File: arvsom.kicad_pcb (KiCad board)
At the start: 12 copper layers, 55 x 40 mm, 451 parts, among them J1 TAG-10PIN, J3 DF40C-100DP-0.4V(51), J4 DF40C-100DP-0.4V(51), Q1 DMG1013UWQ-7, Q5 DMG1012UW, U1 MT53D1024M32D4DT-053, U10 TDA19988BHN_C1,557, U11 KSZ9031RNXCA, U13 VIC7100, U2 GD25LQ256DWIGR, U3 MT53D1024M32D4DT-053, U4 CSD86330Q3D, U5 LMR62014XMF_NOPB, U6 CSD86330Q3D, U7 STM811RW16F, U8 TPS65086100, Y1 ABM8G-25.000MHZ-18-D2Y-T, Y2 ABM8G-25.000MHZ-18-D2Y-T, Y3 ABM8G-27.000MHZ-18-D2Y-T

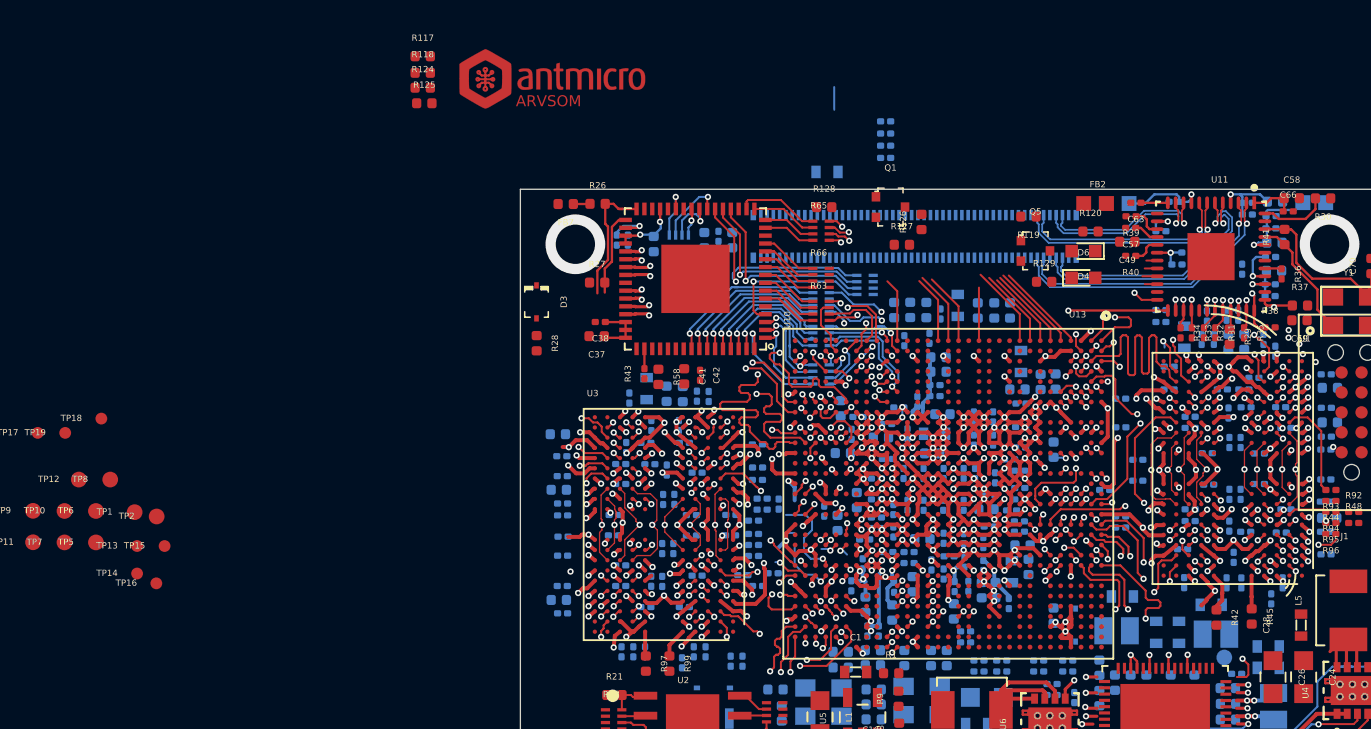
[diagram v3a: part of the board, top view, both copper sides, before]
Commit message: Layout: RGMII, most of LCD
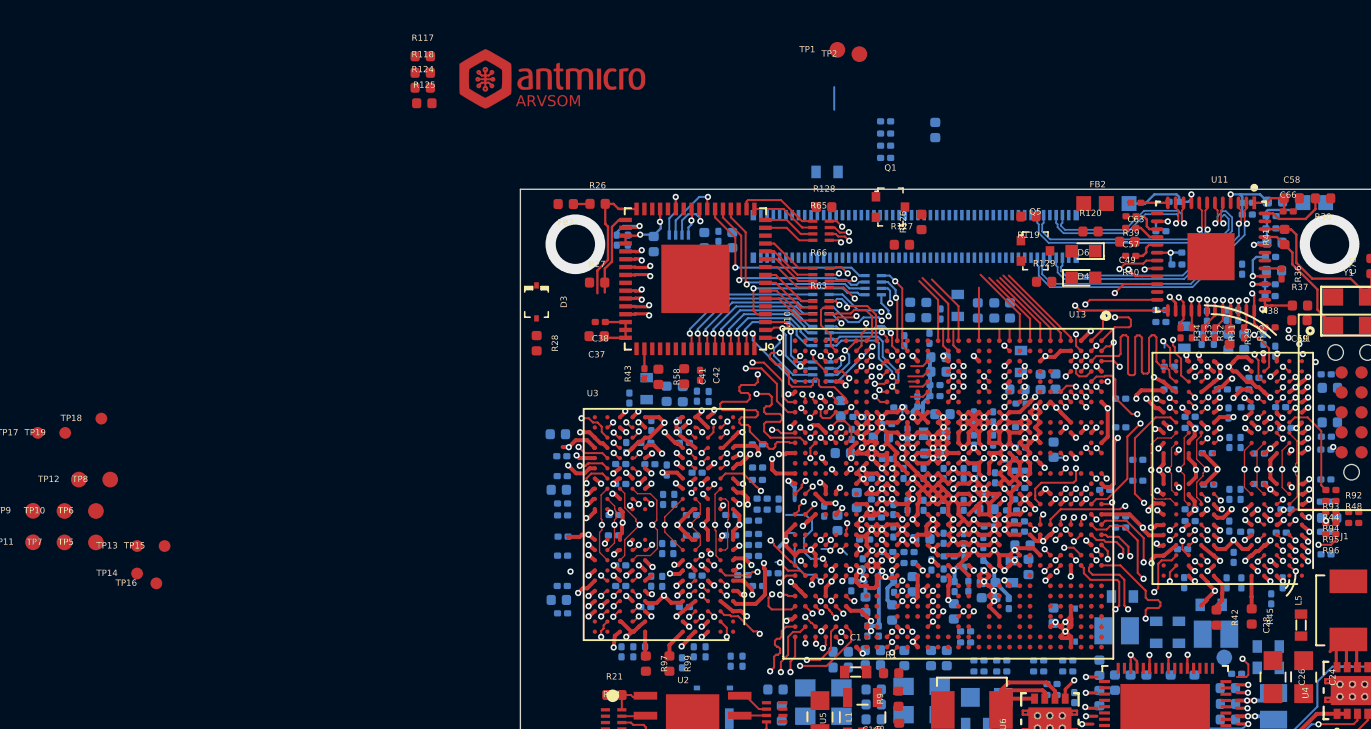
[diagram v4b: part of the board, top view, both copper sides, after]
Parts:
- moved TP1 53.5 mm to (150.2, 46.1)
- moved TP2 53.5 mm to (151.6, 46.4)
- moved C199 11.8 mm to (156.4, 51.2)
- moved R60 0.52 mm to (152.5, 61.1)
- moved R64 0.18 mm to (149.2, 66.6)
- moved R62 0.12 mm to (149.2, 62.3)
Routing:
- net RGMII_MDIO: track 23.3 -> 42.7 mm
- net RGMII_RXCLK: track 19.4 -> 38.2 mm
- net RGMII_MDC: track 21.7 -> 39.0 mm
- net RGMII_RXD1: track 20.4 -> 37.7 mm
- net RGMII_RXD0: track 20.4 -> 35.1 mm
- net RGMII_TXD2: track 17.3 -> 31.9 mm, vias 1 -> 2
- net RGMII_TXD1: track 17.5 -> 32.2 mm, vias 1 -> 2
- net RGMII_RXDV: track 26.5 -> 40.6 mm
- net RGMII_RXD3: track 19.3 -> 33.3 mm
- net RGMII_RXD2: track 20.9 -> 34.0 mm
- net RGMII_GTXCLK: track 18.7 -> 31.6 mm
- net RGMII_TXD0: track 24.4 -> 35.7 mm, vias 1 -> 2
- net RGMII_TXEN: track 29.1 -> 35.8 mm
- net Net-(R65-Pad6): track 3.47 -> 10.1 mm
- net Net-(R60-Pad7): track 0.00 -> 6.51 mm, vias 0 -> 2
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
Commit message: Layout: GPIO breakout
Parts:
- moved C110 5.05 mm to (163.5, 70.7)
- moved C115 0.66 mm to (161.4, 68.3), turned to 270 degrees
- moved C161 0.14 mm to (163.1, 67.3)
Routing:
- net Net-(R20-Pad8): track 0.00 -> 17.3 mm, vias 0 -> 1
- net Net-(R20-Pad5): track 0.46 -> 16.1 mm
- net GPIO13: track 0.46 -> 15.9 mm, vias 1 -> 2
- net Net-(R20-Pad6): track 0.73 -> 15.7 mm, vias 0 -> 1
- net GPIO4: track 0.00 -> 14.4 mm, vias 0 -> 2
- net Net-(R20-Pad7): track 0.65 -> 14.9 mm, vias 0 -> 1
- net GPIO12: track 0.00 -> 13.8 mm, vias 0 -> 2
- net GPIO14: track 0.46 -> 13.5 mm
- net GPIO19: track 0.46 -> 13.4 mm, vias 1 -> 2
- net GPIO5: track 0.00 -> 12.9 mm, vias 0 -> 2
- net GPIO21: track 0.46 -> 13.2 mm, vias 1 -> 2
- net (no net): track 12.5 -> 0.00 mm, vias 6 -> 4
- net GPIO17: track 0.00 -> 12.4 mm, vias 0 -> 2
- net GPIO10: track 0.00 -> 12.2 mm, vias 0 -> 1
- net SDIO0_D0: track 0.46 -> 12.5 mm
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
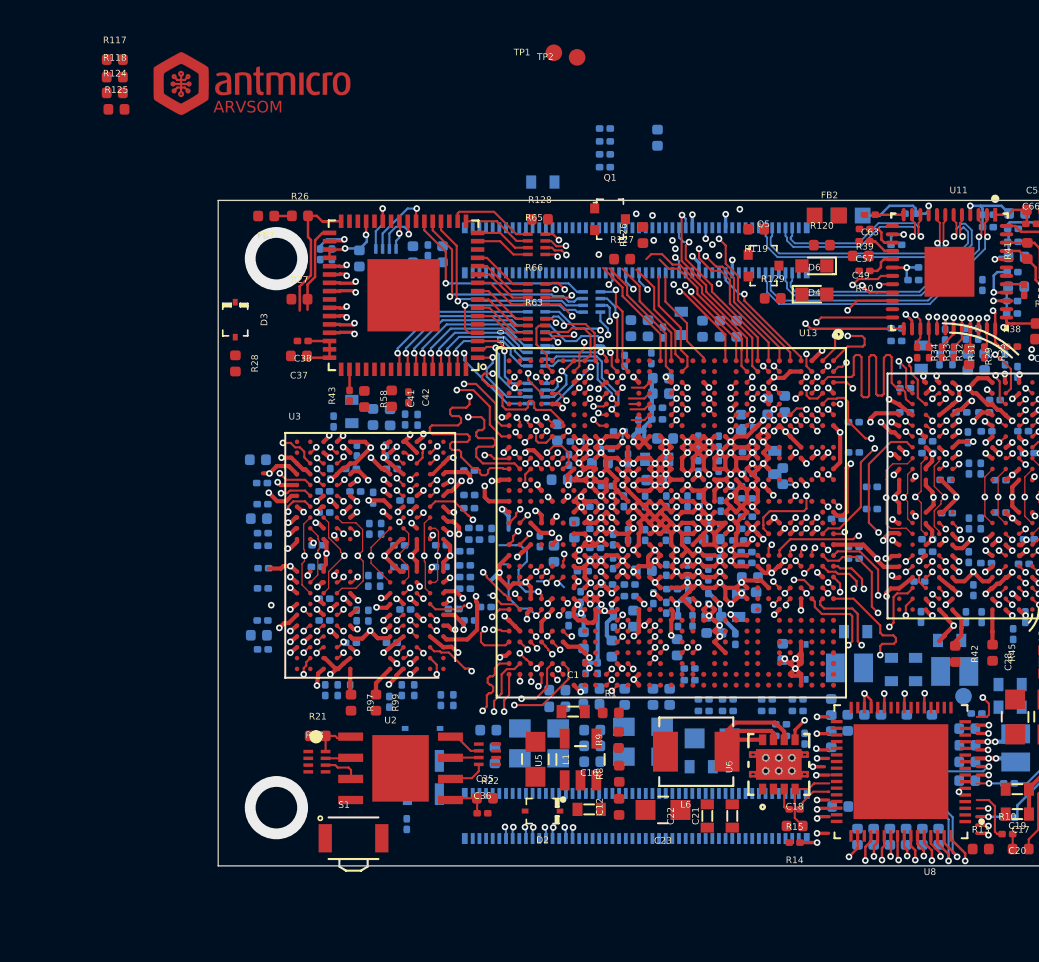
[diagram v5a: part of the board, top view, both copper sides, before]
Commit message: HDMI routed
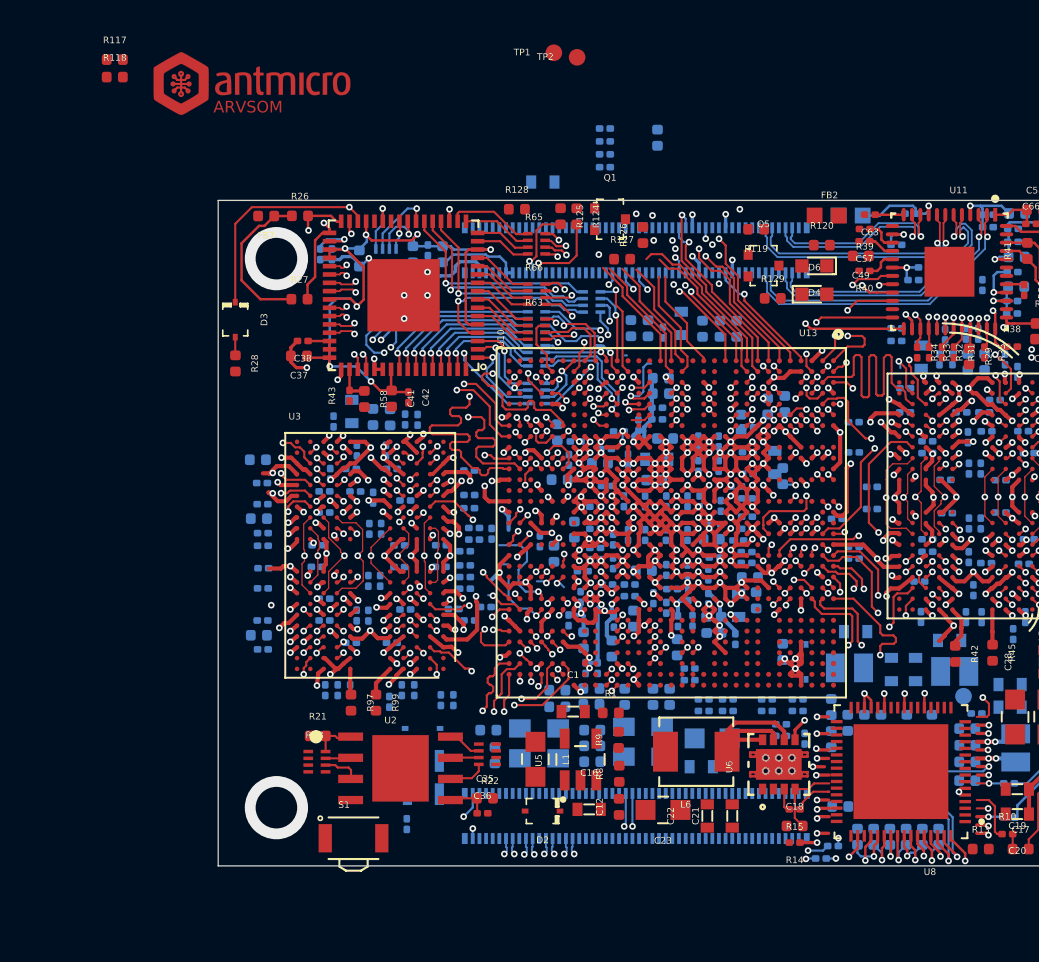
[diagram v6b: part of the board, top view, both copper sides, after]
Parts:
- moved R5 32.2 mm to (166.2, 94.5), turned to 0 degrees
- moved R6 31.3 mm to (167.0, 93.8), turned to 0 degrees
- moved R124 28.7 mm to (151.6, 55.9), turned to 270 degrees
- moved R125 27.5 mm to (150.6, 55.9), turned to 270 degrees
- moved R128 1.51 mm to (148.0, 55.5)
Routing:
- net I2C0_SDA: track 1.39 -> 87.7 mm, vias 0 -> 3
- net I2C0_SCL: track 0.57 -> 85.8 mm, vias 0 -> 3
- net HDMI_CEC: track 0.00 -> 73.8 mm, vias 0 -> 2
- net HDMI_HPD: track 0.00 -> 60.1 mm, vias 0 -> 2
- net HDMI_DSCL: track 5.42 -> 54.0 mm, vias 0 -> 2
- net HDMI_DSDA: track 8.41 -> 51.0 mm, vias 0 -> 2
- net HDMI_TXC_N: track 16.7 -> 53.3 mm
- net HDMI_TXC_P: track 16.5 -> 52.8 mm
- net HDMI_1V8: track 7.88 -> 43.8 mm, vias 2 -> 7
- net HDMI_TX0_N: track 18.1 -> 53.3 mm
- net HDMI_TX0_P: track 17.7 -> 52.8 mm
- net HDMI_TX2_N: track 17.3 -> 50.8 mm
- net HDMI_TX2_P: track 16.9 -> 50.3 mm
- net HDMI_TX1_N: track 16.3 -> 44.1 mm
- net HDMI_TX1_P: track 16.1 -> 43.3 mm
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- added copper zone on GND2, net GND
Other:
- net class eth: clearance 0.1 -> 0.2
